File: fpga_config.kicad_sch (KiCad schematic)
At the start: 12 parts, among them J2 Molex 0878321420, U2 XC7A50T-2FTG256I

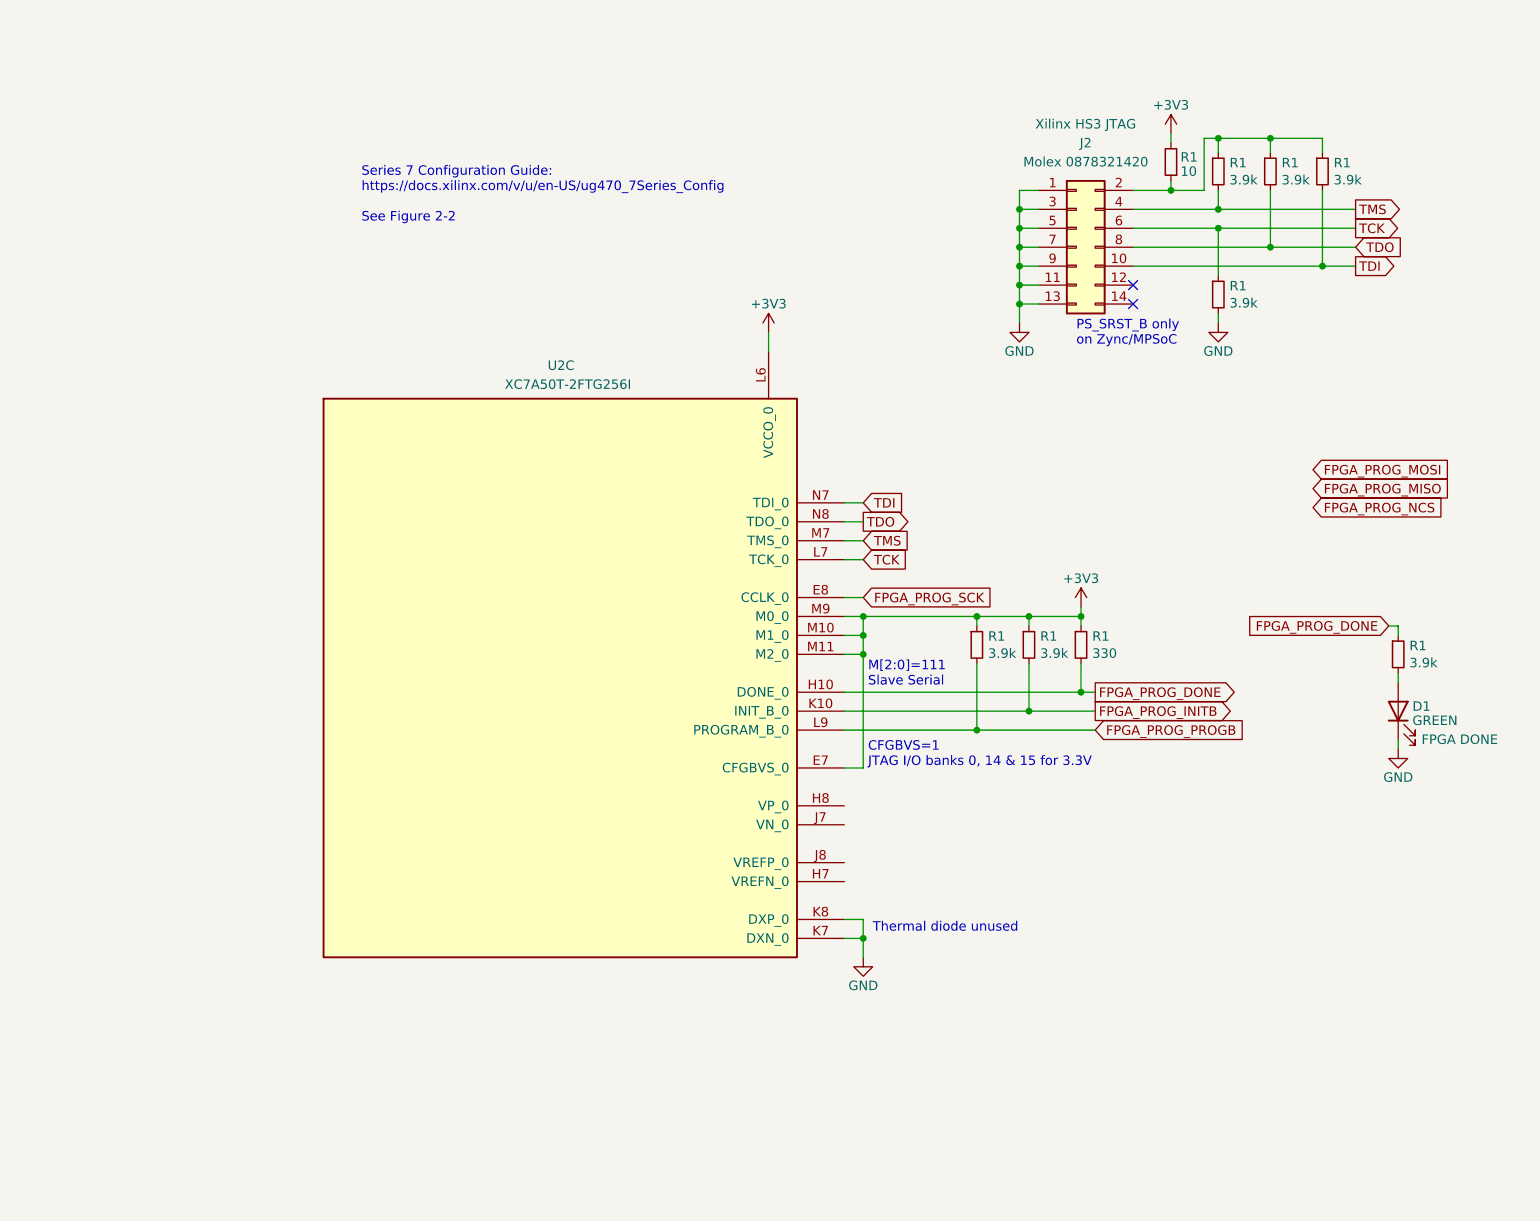
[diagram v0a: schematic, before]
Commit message: Changed FPGA to new package and hooked up some more pins
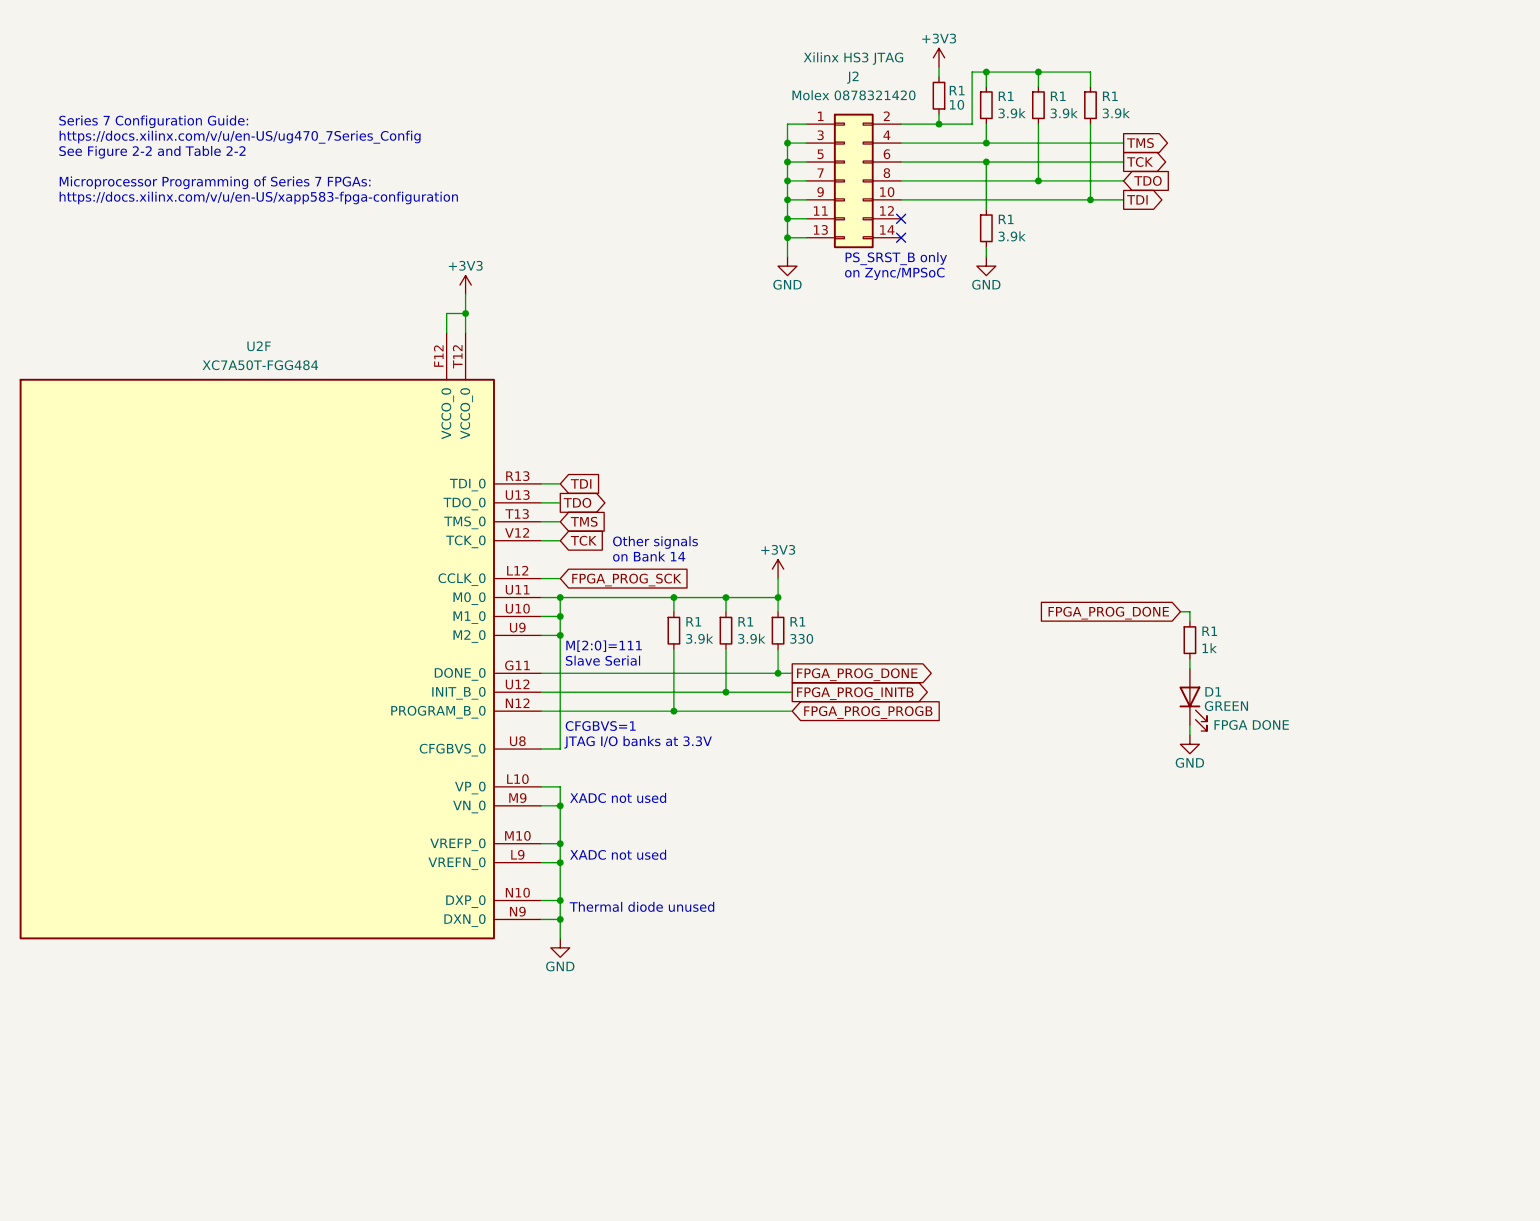
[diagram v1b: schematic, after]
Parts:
- removed U2: XC7A50T-2FTG256I, Package_BGA:Xilinx_FTG256, symbol FPGA_Xilinx_Artix7:XC7A50T-FTG256
- added U2: XC7A50T-FGG484, Package_BGA:Xilinx_FGG484, symbol FPGA_Xilinx_Artix7:XC7A50T-FGG484
- R1: value 3.9k -> 1k; LCSC C23018 -> C21190
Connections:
- net +3V3: now also U2.F12 (VCCO_0), U2.T12 (VCCO_0), U2.U10 (M1_0), U2.U11 (M0_0), U2.U8 (CFGBVS_0), U2.U9 (M2_0)
- net FPGA_PROG_DONE: now also U2.G11 (DONE_0)
- net FPGA_PROG_INITB: now also U2.U12 (INIT_B_0)
- net FPGA_PROG_PROGB: now also U2.N12 (PROGRAM_B_0)
- net FPGA_PROG_SCK: now also U2.L12 (CCLK_0)
- net GND: now also U2.L10 (VP_0), U2.L9 (VREFN_0), U2.M10 (VREFP_0), U2.M9 (VN_0), U2.N10 (DXP_0), U2.N9 (DXN_0)
- net TCK: now also U2.V12 (TCK_0)
- net TDI: now also U2.R13 (TDI_0)
- net TDO: now also U2.U13 (TDO_0)
- net TMS: now also U2.T13 (TMS_0)
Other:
- note added: "CFGBVS=1 JTAG I/O banks at 3.3V"
- note added: "Other signals on Bank 14"
- note added: "Series 7 Configuration Guide: https://docs.xilinx.com/v/u/en-US/ug470_7Series_Config See Figure 2-2 and Table 2-2 Microprocessor Programming of Series 7 FPGAs: https://docs.xilinx.com/v/u/en-US/xapp583-fpga-configuration"
- note added: "XADC not used"
- note removed: "CFGBVS=1 JTAG I/O banks 0, 14 & 15 for 3.3V"
- note removed: "Series 7 Configuration Guide: https://docs.xilinx.com/v/u/en-US/ug470_7Series_Config See Figure 2-2"
- moved on the sheet: D1, J2, R1

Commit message: Schematic finished, starting layout
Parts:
- added C13, C19: 100n, Capacitor_SMD:C_0402_1005Metric_Pad0.74x0.62mm_HandSolder, symbol Device:C_Small
- added C26: 4.7u, Capacitor_SMD:C_0402_1005Metric_Pad0.74x0.62mm_HandSolder, symbol Device:C_Small
- D1: value GREEN -> RED; footprint (none) -> LED_SMD:LED_0603_1608Metric_Pad1.05x0.95mm_HandSolder; LCSC (none) -> C2286
- R10: renamed from R1; footprint Resistor_SMD:R_0603_1608Metric_Pad0.98x0.95mm_HandSolder -> Resistor_SMD:R_0402_1005Metric_Pad0.72x0.64mm_HandSolder; LCSC C23138 -> (none)
- R11: renamed from R1; footprint Resistor_SMD:R_0603_1608Metric_Pad0.98x0.95mm_HandSolder -> Resistor_SMD:R_0402_1005Metric_Pad0.72x0.64mm_HandSolder; LCSC C21190 -> (none)
- R3, R5, R6, R7, R8, R9: renamed from R1; footprint Resistor_SMD:R_0603_1608Metric_Pad0.98x0.95mm_HandSolder -> Resistor_SMD:R_0402_1005Metric_Pad0.72x0.64mm_HandSolder; LCSC C23018 -> (none)
- R4: renamed from R1; footprint Resistor_SMD:R_0603_1608Metric_Pad0.98x0.95mm_HandSolder -> Resistor_SMD:R_0402_1005Metric_Pad0.72x0.64mm_HandSolder; LCSC C22859 -> (none)
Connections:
- net +3V3: now also C13.2, C19.2, C26.2
- net GND: now also C13.1, C19.1, C26.1
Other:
- note added: "(active low indicates FPGA ready to receive bitstream)"
- note added: "(active low reset to configuration logic - clears FPGA)"
- note added: "(configuration clock)"
- note added: "(indicates that config is complete)"
- note added: "Programming Pseudocode 1) Pulse PROGRAM_B 2) Check INIT_B = 0 3) Wait for INIT_B = 1 4) Send config bitstream 5) Check INIT_B = 1 (if low, config failed) 6) Send clock for special startup conditions 7) Check DONE = 1 (if low, startup timeout) 8) Supply 8 further clock cycles (see XAPP583) FPGA reprogramming can be restarted by repeating (1)"
- title: FPGA Configuration (Bank 0) -> FPGA Power
- moved on the sheet: D1, J2, R10, R11, R3, R4, R5, R6, R7, R8, R9, U2F

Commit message: Updated titleblock texts
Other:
- title: FPGA Power -> FPGA Bank 0 (Config)
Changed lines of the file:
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@@
   (paper "A4")
   (title_block
-    (title "FPGA Power")
-    (date "2024-02-11")
+    (title "FPGA Bank 0 (Config)")
+    (date "2024-02-14")
     (rev "0.1")
     (company "George Smart, M1GEO")

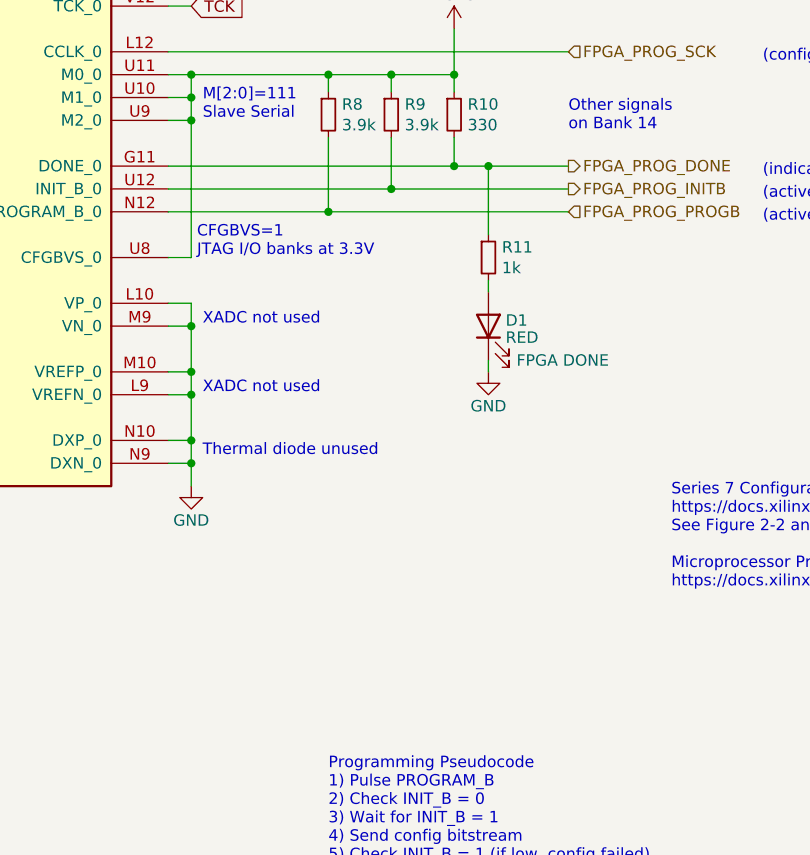
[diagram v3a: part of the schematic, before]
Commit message: Changed linear PSU for SMPS and a few other changes
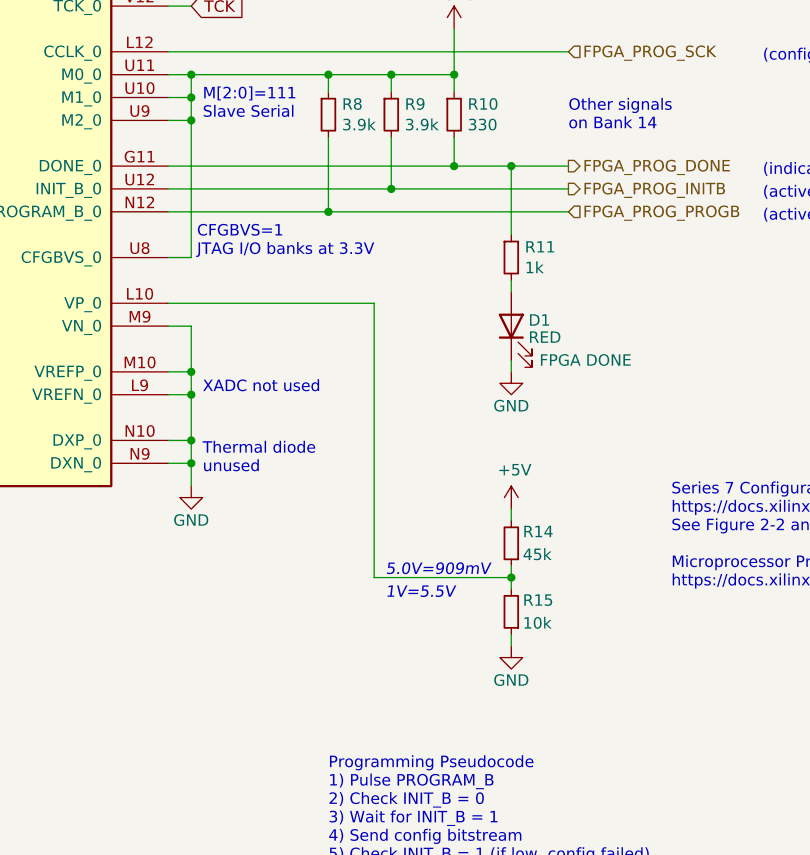
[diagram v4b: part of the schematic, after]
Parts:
- added R14: 45k, Resistor_SMD:R_0402_1005Metric, symbol Device:R_Small
- added R15: 10k, Resistor_SMD:R_0402_1005Metric, symbol Device:R_Small
- D1: footprint LED_SMD:LED_0603_1608Metric_Pad1.05x0.95mm_HandSolder -> LED_SMD:LED_0402_1005Metric; LCSC C2286 -> C965795
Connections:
- net GND: now also R15.1; no longer U2.L10 (VP_0)
- new net: R14.1, R15.2, U2.L10 (VP_0)
- new net +5V: R14.2
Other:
- note added: "1V=5.5V"
- note added: "5.0V=909mV"
- moved on the sheet: D1, R11

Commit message: Started routing. More to go
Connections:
- net +3V3: now also R3.1, R5.1, R6.1
- net 5V_SNS: now reaches R14.1, R15.2, U2.L10 (VP_0)
- new net: J2.2 (Pin_2), R4.1
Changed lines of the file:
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@@
   (junction (at 121.285 85.09) (diameter 0) (color 0 0 0 0)
   )
-  (junction (at 167.005 31.115) (diameter 0) (color 0 0 0 0)
+  (junction (at 167.005 30.48) (diameter 0) (color 0 0 0 0)
   )
   (junction (at 133.35 45.72) (diameter 0) (color 0 0 0 0)
@@
   (junction (at 173.99 48.26) (diameter 0) (color 0 0 0 0)
   )
-  (junction (at 160.02 31.115) (diameter 0) (color 0 0 0 0)
+  (junction (at 160.02 30.48) (diameter 0) (color 0 0 0 0)
   )
   (junction (at 114.3 85.09) (diameter 0) (color 0 0 0 0)
   )
-  (junction (at 153.67 38.1) (diameter 0) (color 0 0 0 0)
-  )
   (junction (at 133.35 53.34) (diameter 0) (color 0 0 0 0)
   )
@@
   )
   (junction (at 86.36 48.26) (diameter 0) (color 0 0 0 0)
+  )
+  (junction (at 153.67 30.48) (diameter 0) (color 0 0 0 0)
   )
   (junction (at 133.35 40.64) (diameter 0) (color 0 0 0 0)
@@
     (stroke (width 0) (type default))
   )
+  (wire (pts (xy 153.67 30.48) (xy 153.67 31.75))
+    (stroke (width 0) (type default))
+  )
   (wire (pts (xy 133.35 48.26) (xy 133.35 45.72))
     (stroke (width 0) (type default))
@@
     (stroke (width 0) (type default))
   )
-  (wire (pts (xy 167.005 31.115) (xy 173.99 31.115))
+  (wire (pts (xy 167.005 30.48) (xy 173.99 30.48))
     (stroke (width 0) (type default))
   )
@@
     (stroke (width 0) (type default))
   )
-  (wire (pts (xy 167.005 31.115) (xy 167.005 33.02))
+  (wire (pts (xy 167.005 30.48) (xy 167.005 33.02))
     (stroke (width 0) (type default))
   )
@@
     (stroke (width 0) (type default))
   )
-  (wire (pts (xy 153.67 30.48) (xy 153.67 31.75))
+  (wire (pts (xy 153.67 29.21) (xy 153.67 30.48))
     (stroke (width 0) (type default))
   )
@@
     (stroke (width 0) (type default))
   )
-  (wire (pts (xy 173.99 31.115) (xy 173.99 33.02))
+  (wire (pts (xy 173.99 30.48) (xy 173.99 33.02))
     (stroke (width 0) (type default))
   )
@@
     (stroke (width 0) (type default))
   )
-  (wire (pts (xy 160.02 31.115) (xy 167.005 31.115))
+  (wire (pts (xy 160.02 30.48) (xy 167.005 30.48))
     (stroke (width 0) (type default))
   )
@@
     (stroke (width 0) (type default))
   )
-  (wire (pts (xy 160.02 31.115) (xy 160.02 33.02))
+  (wire (pts (xy 160.02 30.48) (xy 160.02 33.02))
     (stroke (width 0) (type default))
   )
@@
     (stroke (width 0) (type default))
   )
-  (wire (pts (xy 153.67 38.1) (xy 158.115 38.1))
-    (stroke (width 0) (type default))
-  )
   (wire (pts (xy 134.62 147.32) (xy 134.62 148.59))
     (stroke (width 0) (type default))
@@
     (stroke (width 0) (type default))
   )
-  (wire (pts (xy 158.115 31.115) (xy 160.02 31.115))
+  (wire (pts (xy 153.67 30.48) (xy 160.02 30.48))
     (stroke (width 0) (type default))
   )
@@
   )
   (wire (pts (xy 96.52 74.93) (xy 99.06 74.93))
-    (stroke (width 0) (type default))
-  )
-  (wire (pts (xy 158.115 38.1) (xy 158.115 31.115))
     (stroke (width 0) (type default))
   )
@@
     (effects (font (size 1.27 1.27)) (justify left bottom))
   )
+  (label "5V_SNS" (at 104.775 110.49 0) (fields_autoplaced)
+    (effects (font (size 1.27 1.27)) (justify left bottom))
+  )
   (global_label "TMS" (shape output) (at 178.435 40.64 0) (fields_autoplaced)
     (effects (font (size 1.27 1.27)) (justify left))
@@
     )
   )
-  (symbol (lib_id "power:+3V3") (at 153.67 30.48 0) (unit 1)
+  (symbol (lib_id "power:+3V3") (at 153.67 29.21 0) (unit 1)
     (in_bom yes) (on_board yes) (dnp no)
-    (property "Reference" "#PWR020" (at 153.67 34.29 0)
-      (effects (font (size 1.27 1.27)) hide)
-    )
-    (property "Value" "+3V3" (at 153.67 26.67 0)
+    (property "Reference" "#PWR020" (at 153.67 33.02 0)
+      (effects (font (size 1.27 1.27)) hide)
+    )
+    (property "Value" "+3V3" (at 153.67 25.4 0)
       (effects (font (size 1.27 1.27)))
     )
-    (property "Footprint" "" (at 153.67 30.48 0)
-      (effects (font (size 1.27 1.27)) hide)
-    )
-    (property "Datasheet" "" (at 153.67 30.48 0)
-      (effects (font (size 1.27 1.27)) hide)
-    )
+    (property "Footprint" "" (at 153.67 29.21 0)
+      (effects (font (size 1.27 1.27)) hide)
+    )
+    (property "Datasheet" "" (at 153.67 29.21 0)
+      (effects (font (size 1.27 1.27)) hide)
+    )

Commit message: More routing and tinkering. Need to do non-MGT decoupling next.
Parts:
- added C21: 100n, Capacitor_SMD:C_0402_1005Metric_Pad0.74x0.62mm_HandSolder, symbol Device:C_Small
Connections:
- net +3V3: now also C21.2
- net GND: now also C21.1
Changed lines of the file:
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@@
   (junction (at 167.005 30.48) (diameter 0) (color 0 0 0 0)
+  )
+  (junction (at 173.99 30.48) (diameter 0) (color 0 0 0 0)
   )
   (junction (at 133.35 45.72) (diameter 0) (color 0 0 0 0)
@@
     (stroke (width 0) (type default))
   )
+  (wire (pts (xy 184.15 31.75) (xy 184.15 30.48))
+    (stroke (width 0) (type default))
+  )
   (wire (pts (xy 167.005 30.48) (xy 167.005 33.02))
     (stroke (width 0) (type default))
@@
     (stroke (width 0) (type default))
   )
+  (wire (pts (xy 173.99 30.48) (xy 177.8 30.48))
+    (stroke (width 0) (type default))
+  )
   (wire (pts (xy 96.52 105.41) (xy 99.06 105.41))
     (stroke (width 0) (type default))
@@
   )
   (wire (pts (xy 173.99 48.26) (xy 178.435 48.26))
+    (stroke (width 0) (type default))
+  )
+  (wire (pts (xy 182.88 30.48) (xy 184.15 30.48))
     (stroke (width 0) (type default))
   )
@@
     )
   )
+  (symbol (lib_id "power:GND") (at 184.15 31.75 0) (mirror y) (unit 1)
+    (in_bom yes) (on_board yes) (dnp no)
+    (property "Reference" "#PWR050" (at 184.15 38.1 0)
+      (effects (font (size 1.27 1.27)) hide)
+    )
+    (property "Value" "GND" (at 184.15 35.56 0)
+      (effects (font (size 1.27 1.27)))
+    )
+    (property "Footprint" "" (at 184.15 31.75 0)
+      (effects (font (size 1.27 1.27)) hide)
+    )
+    (property "Datasheet" "" (at 184.15 31.75 0)
+      (effects (font (size 1.27 1.27)) hide)
+    )
+    (pin "1")
+    (instances
+      (project "Pi5-Artix50T-Hat"
+        (path "/e63e39d7-6ac0-4ffd-8aa3-1841a4541b55/58f29d61-b732-4149-afb6-3ea37966fd1b/d2024c52-5905-49ab-a9c8-6dd77f08fcfb"
+          (reference "#PWR050") (unit 1)
+        )
+      )
+    )
+  )
   (symbol (lib_id "power:+5V") (at 134.62 133.35 0) (unit 1)
     (in_bom yes) (on_board yes) (dnp no)
@@
         )
       )
+    )
+  )
+  (symbol (lib_id "Device:C_Small") (at 180.34 30.48 270) (unit 1)
+    (in_bom yes) (on_board yes) (dnp no)
+    (property "Reference" "C21" (at 180.34 24.765 90)
+      (effects (font (size 1.27 1.27)))
+    )
+    (property "Value" "100n" (at 180.34 27.305 90)
+      (effects (font (size 1.27 1.27)))
+    )
+    (property "Footprint" "Capacitor_SMD:C_0402_1005Metric_Pad0.74x0.62mm_HandSolder" (at 180.34 30.48 0)
+      (effects (font (size 1.27 1.27)) hide)
+    )
+    (property "Datasheet" "https://datasheet.lcsc.com/lcsc/2304140030_Samsung-Electro-Mechanics-CL05B104KO5NNNC_C1525.pdf" (at 180.34 30.48 0)
+      (effects (font (size 1.27 1.27)) hide)
+    )
+    (property "LCSC" "C1525" (at 180.34 30.48 90)
+      (effects (font (size 1.27 1.27)) hide)
+    )
+    (pin "2")
+    (pin "1")
+    (instances
+      (project "Pi5-Artix50T-Hat"
+        (path "/e63e39d7-6ac0-4ffd-8aa3-1841a4541b55/58f29d61-b732-4149-afb6-3ea37966fd1b/d2024c52-5905-49ab-a9c8-6dd77f08fcfb"
+          (reference "C21") (unit 1)
+        )
+      )
